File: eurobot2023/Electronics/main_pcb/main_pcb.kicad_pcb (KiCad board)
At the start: 2 copper layers, 88 x 94 mm, 55 parts, among them IC1 CD74HCT125M96, IC2 SN74LVC126ADR, J1 PI40HAT, J10 Conn_01x02_Male, J11 MagneticEncoder, J12 Conn_01x07_Male, J13 MagneticEncoder, J14 Conn_01x03_Male, J15 Conn_01x02_Male, J16 Conn_02x02_Odd_Even, J17 Conn_02x02_Odd_Even, J18 Conn_02x02_Odd_Even, J2 Conn_01x02_Male, J20 Conn_01x03_Male, J21 Conn_01x03_Male, J24 Conn_01x03_Male, J3 Conn_01x02_Male, J4 Conn_01x02_Male, J5 Conn_01x02_Male, J6 Conn_01x02_Male, J7 Conn_01x02_Male, J8 Conn_01x02_Male, J9 22-03-5035, P1 R-78Bxx-2.0, P2 Amazon 10A stepdown, Q1 2SK4017_Q_, Q2 2SK4017_Q_, Q3 2SK4017_Q_, Q4 2SK4017_Q_, Q5 2SK4017_Q_, Q6 2SK4017_Q_, U1 MCP2515-xSO, U2 TJA1049T, U3 PCA9306D, U4 Pololu_MAX14870, U5 PCA9685PW, U6 Pololu_MAX14870

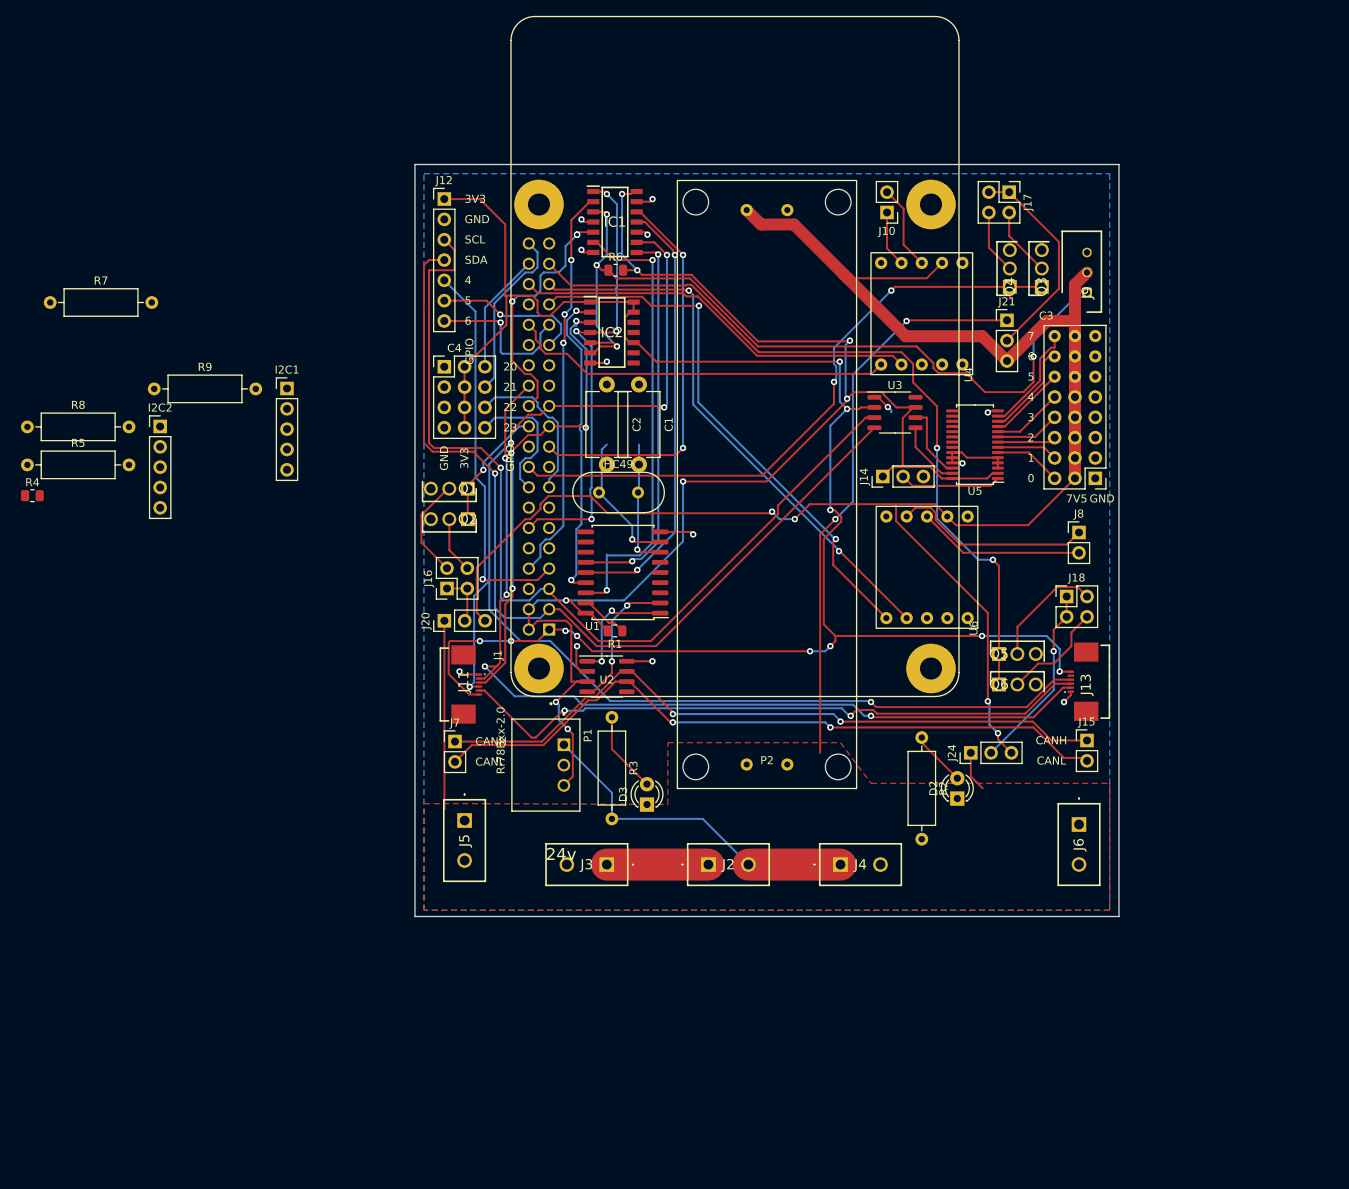
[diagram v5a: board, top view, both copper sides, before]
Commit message: Electronics: update PCB
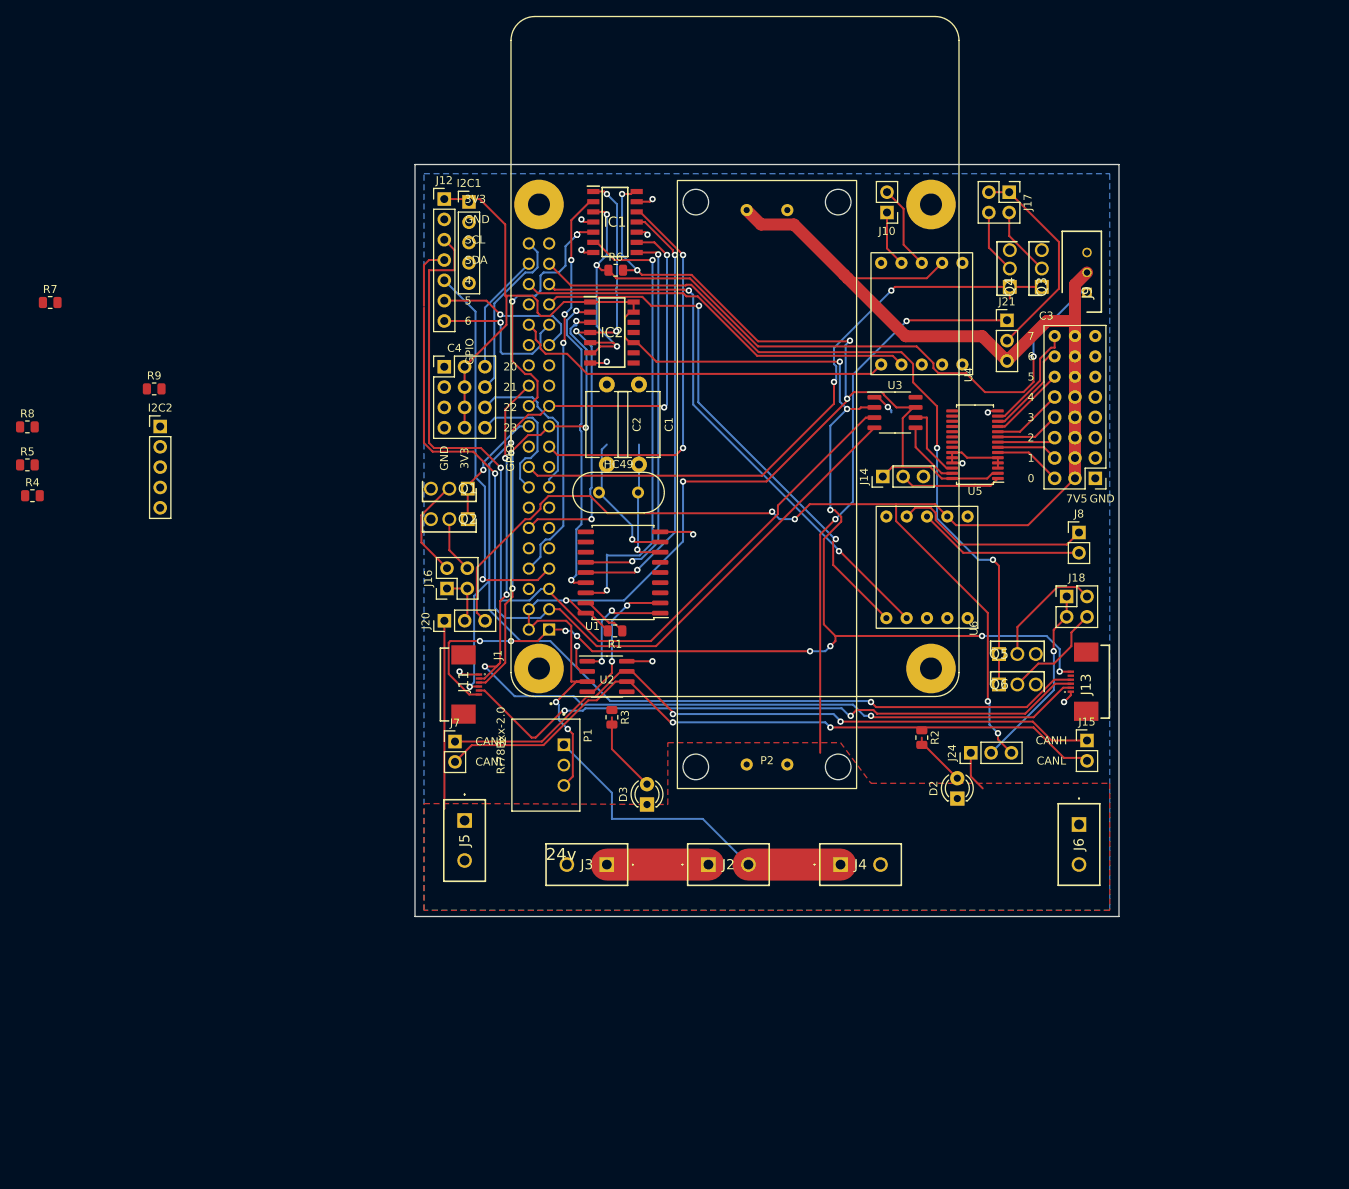
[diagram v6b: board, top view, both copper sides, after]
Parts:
- R2, R3, R5, R7, R8, R9: footprint Resistor_THT:R_Axial_DIN0309_L9.0mm_D3.2mm_P12.70mm_Horizontal -> Resistor_SMD:R_0805_2012Metric
- moved I2C1 32.6 mm to (76.8, 60.7)
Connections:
- J11 pad 1: GND -> +3.3V
- J11 pad 2: /SPI1_CS1 -> Net-(J11-Pad2)
- J11 pad 3: /SPI1 MISO -> /SPI1 CLK
- J11 pad 4: /SPI1 CLK -> /SPI1 MISO
- J11 pad 5: Net-(J11-Pad5) -> /SPI1_CS1
- J11 pad 6: +3.3V -> GND
- J13 pad 1: GND -> +3.3V
- J13 pad 2: /SPI1_CS1 -> unconnected-(J13-Pad2)
- J13 pad 3: Net-(J11-Pad5) -> /SPI1 CLK
- J13 pad 4: /SPI1 CLK -> Net-(J11-Pad2)
- J13 pad 5: unconnected-(J13-Pad5) -> /SPI1_CS1
- J13 pad 6: +3.3V -> GND
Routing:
- net unconnected-(J13-Pad2): track 0.00 -> 118.9 mm, vias 0 -> 4
- net Net-(J11-Pad5): track 80.4 -> 0.00 mm, vias 2 -> 0
- net /SPI1_CS1: track 118.9 -> 80.4 mm, vias 4 -> 2
- net Net-(J2-Pad2): track 42.7 -> 52.9 mm
- net Net-(D3-Pad2): track 10.2 -> 0.00 mm
- net GND: track 39.2 -> 35.0 mm, vias 13 -> 11
- net +3.3V: track 222.9 -> 227.1 mm, vias 11 -> 13

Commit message: Correct main pcb routes
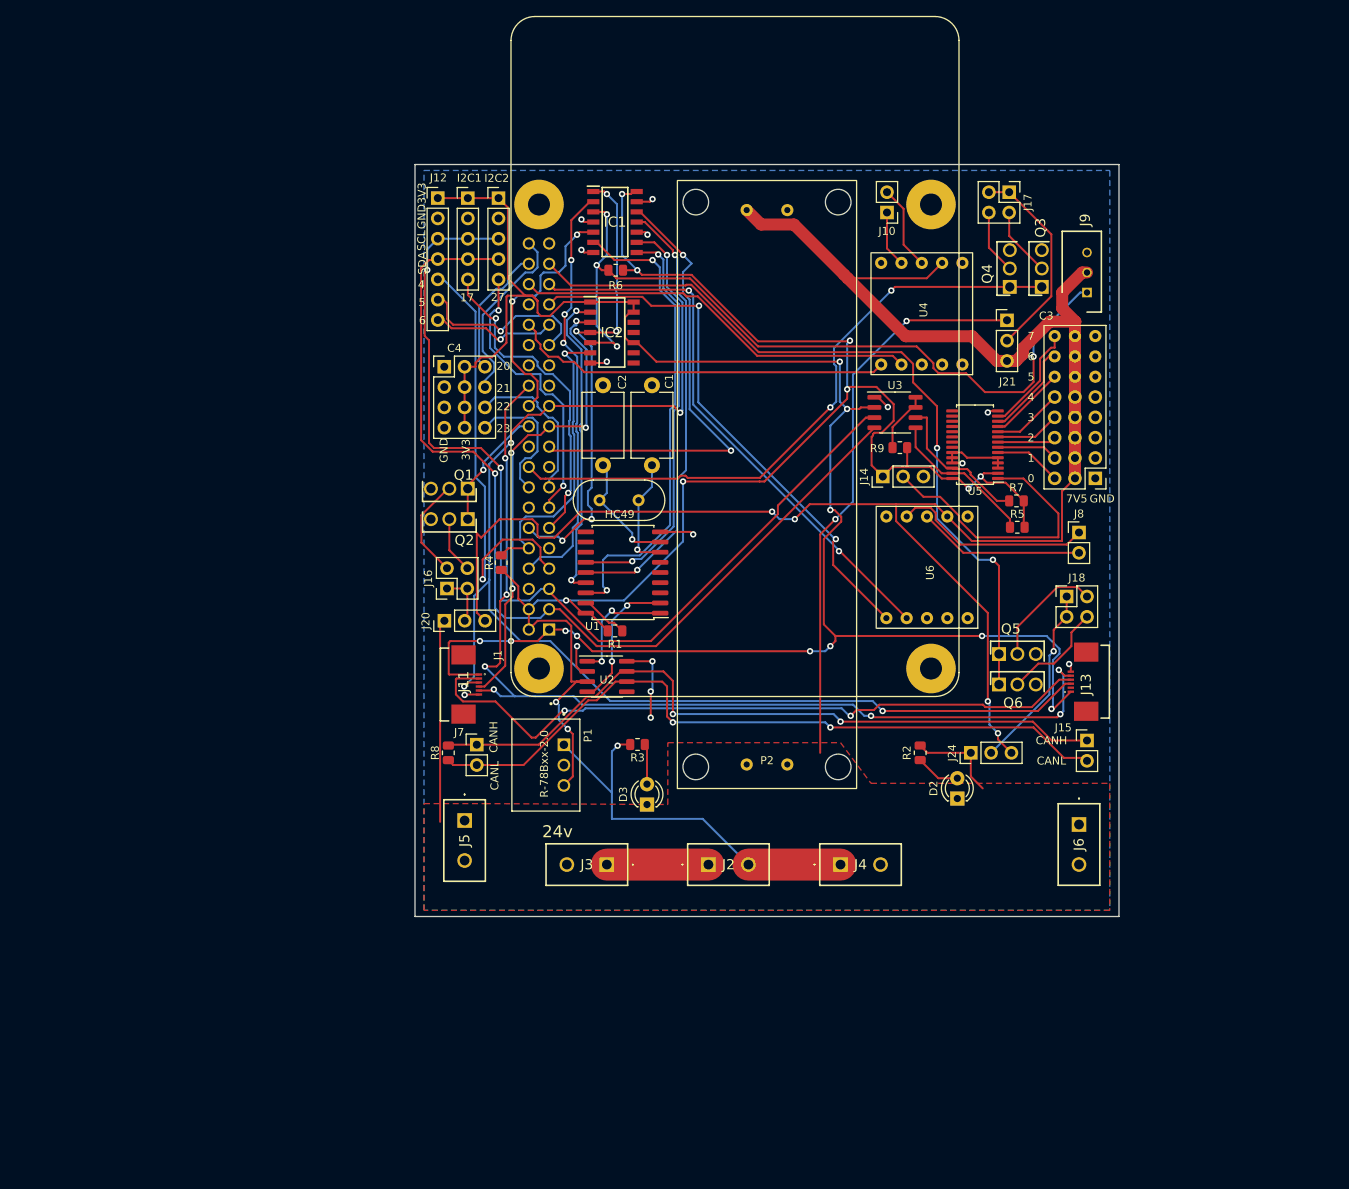
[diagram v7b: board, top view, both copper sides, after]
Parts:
- moved R5 124.0 mm to (145.3, 101.3)
- moved R7 123.3 mm to (145.2, 98.0)
- moved R9 93.5 mm to (130.6, 91.4)
- moved R8 66.5 mm to (74.2, 129.5), turned to 90 degrees
- moved R4 59.2 mm to (80.8, 105.8), turned to -90 degrees
- moved I2C2 51.0 mm to (80.4, 60.2)
- moved R3 4.67 mm to (97.8, 128.5), turned to 180 degrees
- moved J7 2.75 mm to (77.7, 128.5)
- moved R2 1.91 mm to (133.1, 129.5), turned to 90 degrees
- moved C1 1.62 mm to (99.6, 83.6)
- moved HC49 0.97 mm to (93.1, 98.0)
- moved J12 0.82 mm to (72.8, 60.2)
- moved I2C1 0.49 mm to (76.6, 60.2)
- moved C2 0.49 mm to (93.5, 83.6)
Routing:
- net unconnected-(J13-Pad2): track 118.9 -> 0.00 mm, vias 4 -> 0
- net Net-(J11-Pad2): track 0.00 -> 87.9 mm, vias 0 -> 2
- net /SPI1_CS1: track 80.4 -> 125.7 mm, vias 2 -> 7
- net /GPIO 17: track 0.00 -> 40.6 mm, vias 0 -> 2
- net /UART_RX: track 0.00 -> 37.2 mm, vias 0 -> 1
- net /GPIO 27: track 0.00 -> 36.1 mm, vias 0 -> 2
- net /A0: track 12.7 -> 35.2 mm
- net +5V: track 182.4 -> 201.6 mm, vias 8 -> 10
- net Net-(R5-Pad1): track 8.35 -> 19.0 mm
- net GND: track 35.0 -> 44.1 mm, vias 11 -> 15
- net /SPI1 MOSI: track 49.7 -> 58.8 mm
- net Net-(R7-Pad1): track 9.44 -> 18.4 mm
- net +7.5V: track 220.7 -> 229.5 mm
- net +24V: track 99.6 -> 108.2 mm
- net +3.3V: track 227.1 -> 235.3 mm, vias 13 -> 11
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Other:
- board text added: "17"
- board text added: "27"
- board text removed: "GPIO"

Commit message: Fix main pcb
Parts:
- removed I2C1, I2C2: Conn_01x05_Male, Connector_PinHeader_2.54mm:PinHeader_1x05_P2.54mm_Vertical
- removed J12: Conn_01x07_Male, Connector_PinHeader_2.54mm:PinHeader_1x07_P2.54mm_Vertical
- added C5: Conn_03x05, MiAM:Pin_Header_Straight_3x05_Pitch2.54mm, F.Cu at (73.4, 59.6)
- added R10: 10k, Resistor_SMD:R_0805_2012Metric, F.Cu at (74.3, 93.8)
- added R11: 10k, Resistor_SMD:R_0805_2012Metric, F.Cu at (147.5, 74.0)
- added R12: 10k, Resistor_SMD:R_0805_2012Metric, F.Cu at (145.7, 109.3)
- moved C1 0.26 mm to (99.4, 83.6)
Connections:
- R4 pad 2: +5V -> +3.3V
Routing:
- net GND: track 44.1 -> 59.2 mm, vias 15 -> 16
- net +3.3V: track 235.3 -> 245.3 mm
- net +5V: track 201.6 -> 195.2 mm
- net /GPIO 24: track 79.2 -> 82.7 mm
- net /GPIO 25: track 15.5 -> 18.7 mm
- net /I2C SDA: track 121.8 -> 119.3 mm
- net Net-(J21-Pad2): track 25.6 -> 23.2 mm
- net /I2C SCL: track 123.2 -> 121.6 mm
- net /GPIO 27: track 36.1 -> 37.6 mm
- net /GPIO 5: track 21.7 -> 20.6 mm
- net /GPIO 17: track 40.6 -> 41.6 mm
- net /GPIO 26: track 96.3 -> 97.1 mm
